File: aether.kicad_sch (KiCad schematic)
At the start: 41 parts, among them J2 USB_C_Receptacle_USB2.0, Q1 NPN, Q2 NPN, Q3 NPN, Q4 NPN, Q5 NPN, SW1 SW_SPDT, SW3 SW_Push, U13 STM32F405RGTx, U4 USBLC6-2SC6, Y1 25MHz

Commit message: updated footprint library
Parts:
- C24, C25, C26, C27, C28, C35, C42: footprint Capacitor_SMD:C_0201_0603Metric -> Capacitor_SMD:C_0402_1005Metric
- C36, C41: footprint (none) -> Capacitor_SMD:C_0402_1005Metric
- R10, R9: footprint Resistor_SMD:R_0201_0603Metric -> Resistor_SMD:R_0402_1005Metric
- R33, R35, R37, R39, R41, R42, R43, R44, R52: footprint (none) -> Resistor_SMD:R_0402_1005Metric
- RN1: footprint (none) -> 742C083274JP:RESCAV80P320X160X70-8N
- RN2: footprint (none) -> YC164-JR-0747KL:RESCAXE80P320X160X70-8N
- RN4: footprint (none) -> YC164-JR-0710KL:RESCAXE80P320X160X70-8N
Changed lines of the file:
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@@
       (effects (font (size 1.27 1.27)))
     )
-    (property "Footprint" "" (at 243.84 104.775 90)
+    (property "Footprint" "YC164-JR-0710KL:RESCAXE80P320X160X70-8N" (at 243.84 104.775 90)
       (effects (font (size 1.27 1.27)) hide)
     )
@@
       (effects (font (size 1.27 1.27)) (justify left))
     )
-    (property "Footprint" "Capacitor_SMD:C_0201_0603Metric" (at 51.7652 186.69 0)
+    (property "Footprint" "Capacitor_SMD:C_0402_1005Metric" (at 51.7652 186.69 0)
       (effects (font (size 1.27 1.27)) hide)
     )
@@
       (effects (font (size 1.27 1.27)))
     )
-    (property "Footprint" "" (at 145.7452 110.49 0)
+    (property "Footprint" "Capacitor_SMD:C_0402_1005Metric" (at 145.7452 110.49 0)
       (effects (font (size 1.27 1.27)) hide)
     )
@@
       (effects (font (size 1.27 1.27)) (justify left))
     )
-    (property "Footprint" "" (at 143.002 97.79 90)
+    (property "Footprint" "Resistor_SMD:R_0402_1005Metric" (at 143.002 97.79 90)
       (effects (font (size 1.27 1.27)) hide)
     )
@@
       (effects (font (size 1.27 1.27)) (justify left))
     )
-    (property "Footprint" "Capacitor_SMD:C_0201_0603Metric" (at 105.1052 186.69 0)
+    (property "Footprint" "Capacitor_SMD:C_0402_1005Metric" (at 105.1052 186.69 0)
       (effects (font (size 1.27 1.27)) hide)
     )
@@
       (effects (font (size 1.27 1.27)))
     )
-    (property "Footprint" "" (at 243.84 125.222 90)
+    (property "Footprint" "Resistor_SMD:R_0402_1005Metric" (at 243.84 125.222 90)
       (effects (font (size 1.27 1.27)) hide)
     )
@@
       (effects (font (size 1.27 1.27)) (justify left))
     )
-    (property "Footprint" "Capacitor_SMD:C_0201_0603Metric" (at 202.8952 144.78 0)
+    (property "Footprint" "Capacitor_SMD:C_0402_1005Metric" (at 202.8952 144.78 0)
       (effects (font (size 1.27 1.27)) hide)
     )
@@
       (effects (font (size 1.27 1.27)) (justify left))
     )
-    (property "Footprint" "" (at 252.095 45.72 90)
+    (property "Footprint" "YC164-JR-0747KL:RESCAXE80P320X160X70-8N" (at 252.095 45.72 90)
       (effects (font (size 1.27 1.27)) hide)
     )
@@
       (effects (font (size 1.27 1.27)))
     )
-    (property "Footprint" "" (at 243.84 141.732 90)
+    (property "Footprint" "Resistor_SMD:R_0402_1005Metric" (at 243.84 141.732 90)
       (effects (font (size 1.27 1.27)) hide)
     )
@@
       (effects (font (size 1.27 1.27)))
     )
-    (property "Footprint" "Resistor_SMD:R_0201_0603Metric" (at 204.47 42.418 90)
+    (property "Footprint" "Resistor_SMD:R_0402_1005Metric" (at 204.47 42.418 90)
       (effects (font (size 1.27 1.27)) hide)
     )
@@
       (effects (font (size 1.27 1.27)) (justify left))
     )
-    (property "Footprint" "Capacitor_SMD:C_0201_0603Metric" (at 148.2852 185.42 0)
+    (property "Footprint" "Capacitor_SMD:C_0402_1005Metric" (at 148.2852 185.42 0)
       (effects (font (size 1.27 1.27)) hide)
     )
@@
       (effects (font (size 1.27 1.27)))
     )
-    (property "Footprint" "" (at 243.84 97.282 90)
+    (property "Footprint" "Resistor_SMD:R_0402_1005Metric" (at 243.84 97.282 90)
       (effects (font (size 1.27 1.27)) hide)
     )
@@
       (effects (font (size 1.27 1.27)))
     )
-    (property "Footprint" "" (at 255.27 42.545 90)
+    (property "Footprint" "742C083274JP:RESCAV80P320X160X70-8N" (at 255.27 42.545 90)
       (effects (font (size 1.27 1.27)) hide)
     )
@@
       (effects (font (size 1.27 1.27)))
     )
-    (property "Footprint" "" (at 193.04 94.488 90)
+    (property "Footprint" "Resistor_SMD:R_0402_1005Metric" (at 193.04 94.488 90)
       (effects (font (size 1.27 1.27)) hide)
     )
@@
       (effects (font (size 1.27 1.27)) (justify left))
     )
-    (property "Footprint" "Capacitor_SMD:C_0201_0603Metric" (at 69.5452 186.69 0)
+    (property "Footprint" "Capacitor_SMD:C_0402_1005Metric" (at 69.5452 186.69 0)
       (effects (font (size 1.27 1.27)) hide)
     )
@@
       (effects (font (size 1.27 1.27)) (justify right))
     )
-    (property "Footprint" "" (at 189.738 97.79 90)
+    (property "Footprint" "Resistor_SMD:R_0402_1005Metric" (at 189.738 97.79 90)
       (effects (font (size 1.27 1.27)) hide)
     )
@@
       (effects (font (size 1.27 1.27)))
     )
-    (property "Footprint" "" (at 243.84 80.772 90)
+    (property "Footprint" "Resistor_SMD:R_0402_1005Metric" (at 243.84 80.772 90)
       (effects (font (size 1.27 1.27)) hide)
     )
@@
       (effects (font (size 1.27 1.27)) (justify left))
     )
-    (property "Footprint" "Capacitor_SMD:C_0201_0603Metric" (at 33.9852 186.69 0)
+    (property "Footprint" "Capacitor_SMD:C_0402_1005Metric" (at 33.9852 186.69 0)
       (effects (font (size 1.27 1.27)) hide)
     )
@@
       (effects (font (size 1.27 1.27)))
     )
-    (property "Footprint" "" (at 126.0348 102.87 0)
+    (property "Footprint" "Capacitor_SMD:C_0402_1005Metric" (at 126.0348 102.87 0)
       (effects (font (size 1.27 1.27)) hide)
     )
@@
       (effects (font (size 1.27 1.27)))
     )
-    (property "Footprint" "Resistor_SMD:R_0201_0603Metric" (at 204.47 36.322 90)
+    (property "Footprint" "Resistor_SMD:R_0402_1005Metric" (at 204.47 36.322 90)
       (effects (font (size 1.27 1.27)) hide)
     )
@@
       (effects (font (size 1.27 1.27)))
     )
-    (property "Footprint" "" (at 38.1 121.158 90)
+    (property "Footprint" "Resistor_SMD:R_0402_1005Metric" (at 38.1 121.158 90)
       (effects (font (size 1.27 1.27)) hide)
     )
@@
       (effects (font (size 1.27 1.27)))
     )
-    (property "Footprint" "" (at 121.92 139.192 90)
+    (property "Footprint" "Resistor_SMD:R_0402_1005Metric" (at 121.92 139.192 90)
       (effects (font (size 1.27 1.27)) hide)
     )
@@
       (effects (font (size 1.27 1.27)) (justify left))
     )
-    (property "Footprint" "Capacitor_SMD:C_0201_0603Metric" (at 87.3252 186.69 0)
-      (effects (font (size 1.27 1.27)) hide)
-    )
+    (property "Footprint" "Capacitor_SMD:C_0402_1005Metric" (at 87.3252 186.69 0)
+      (effects (font (size 1.27 1.27)) hide)
+    )

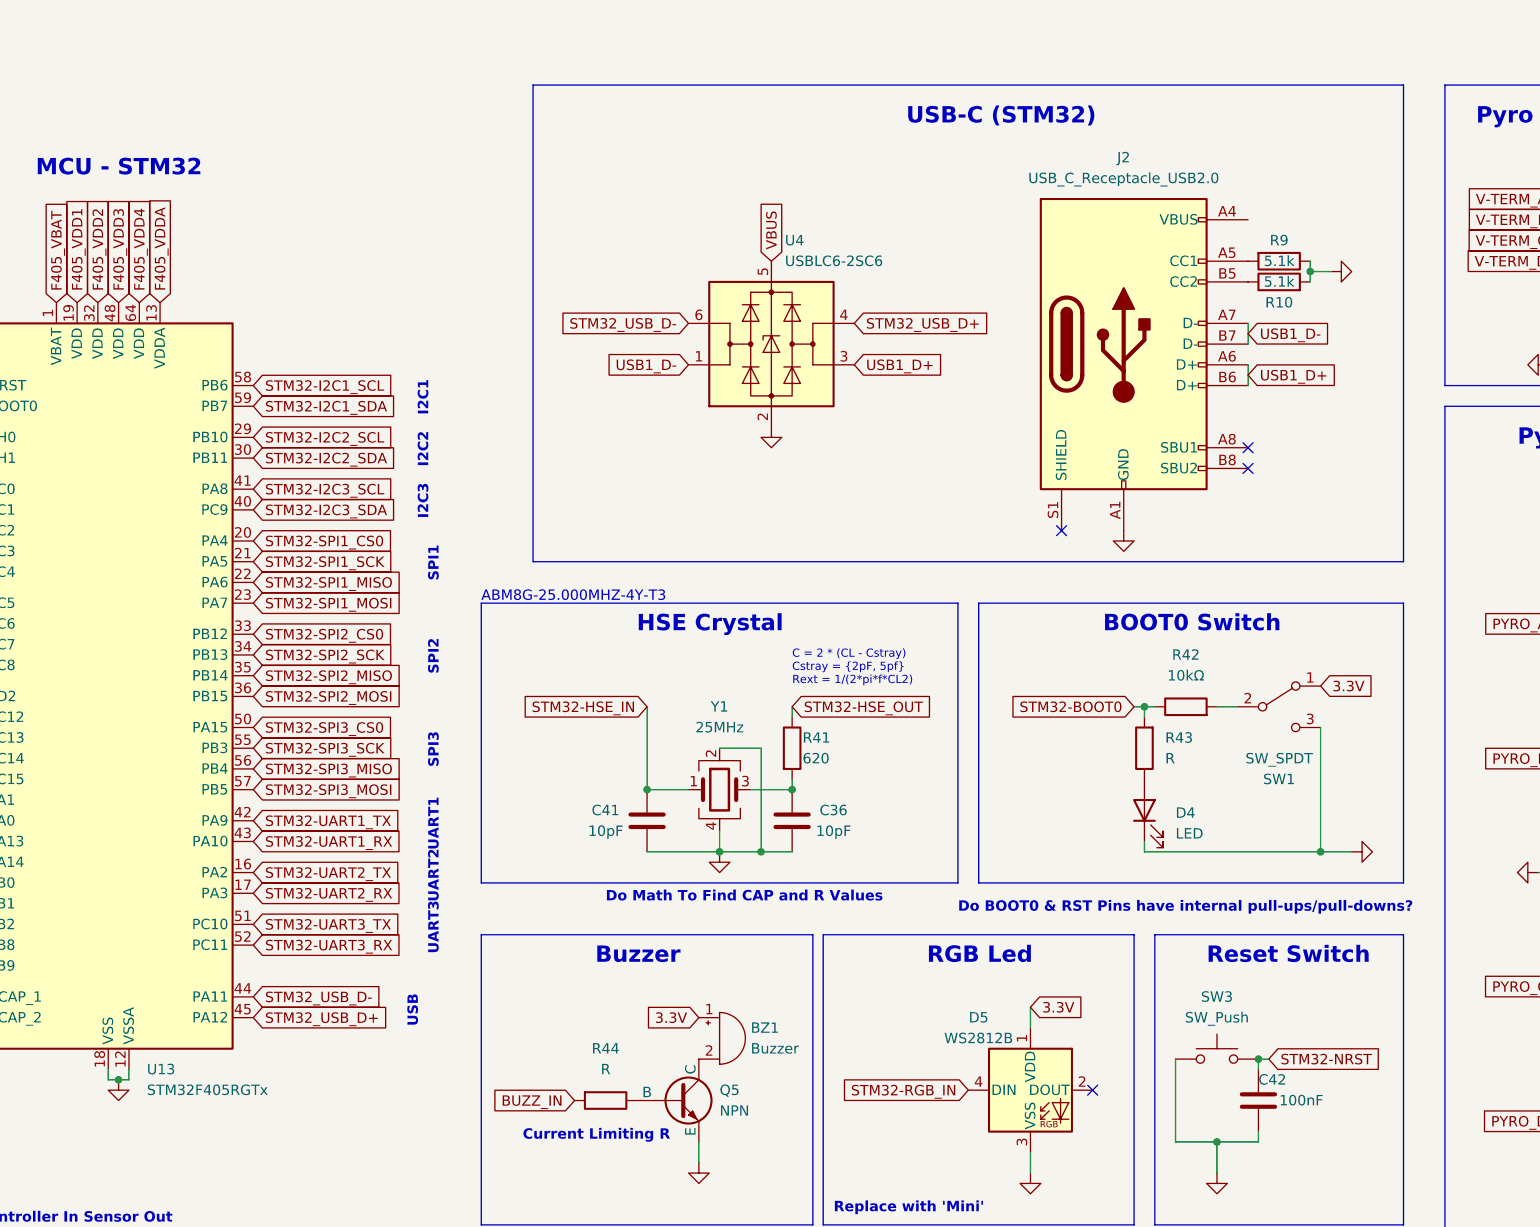
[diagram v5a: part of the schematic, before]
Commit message: Updated symbol footprints
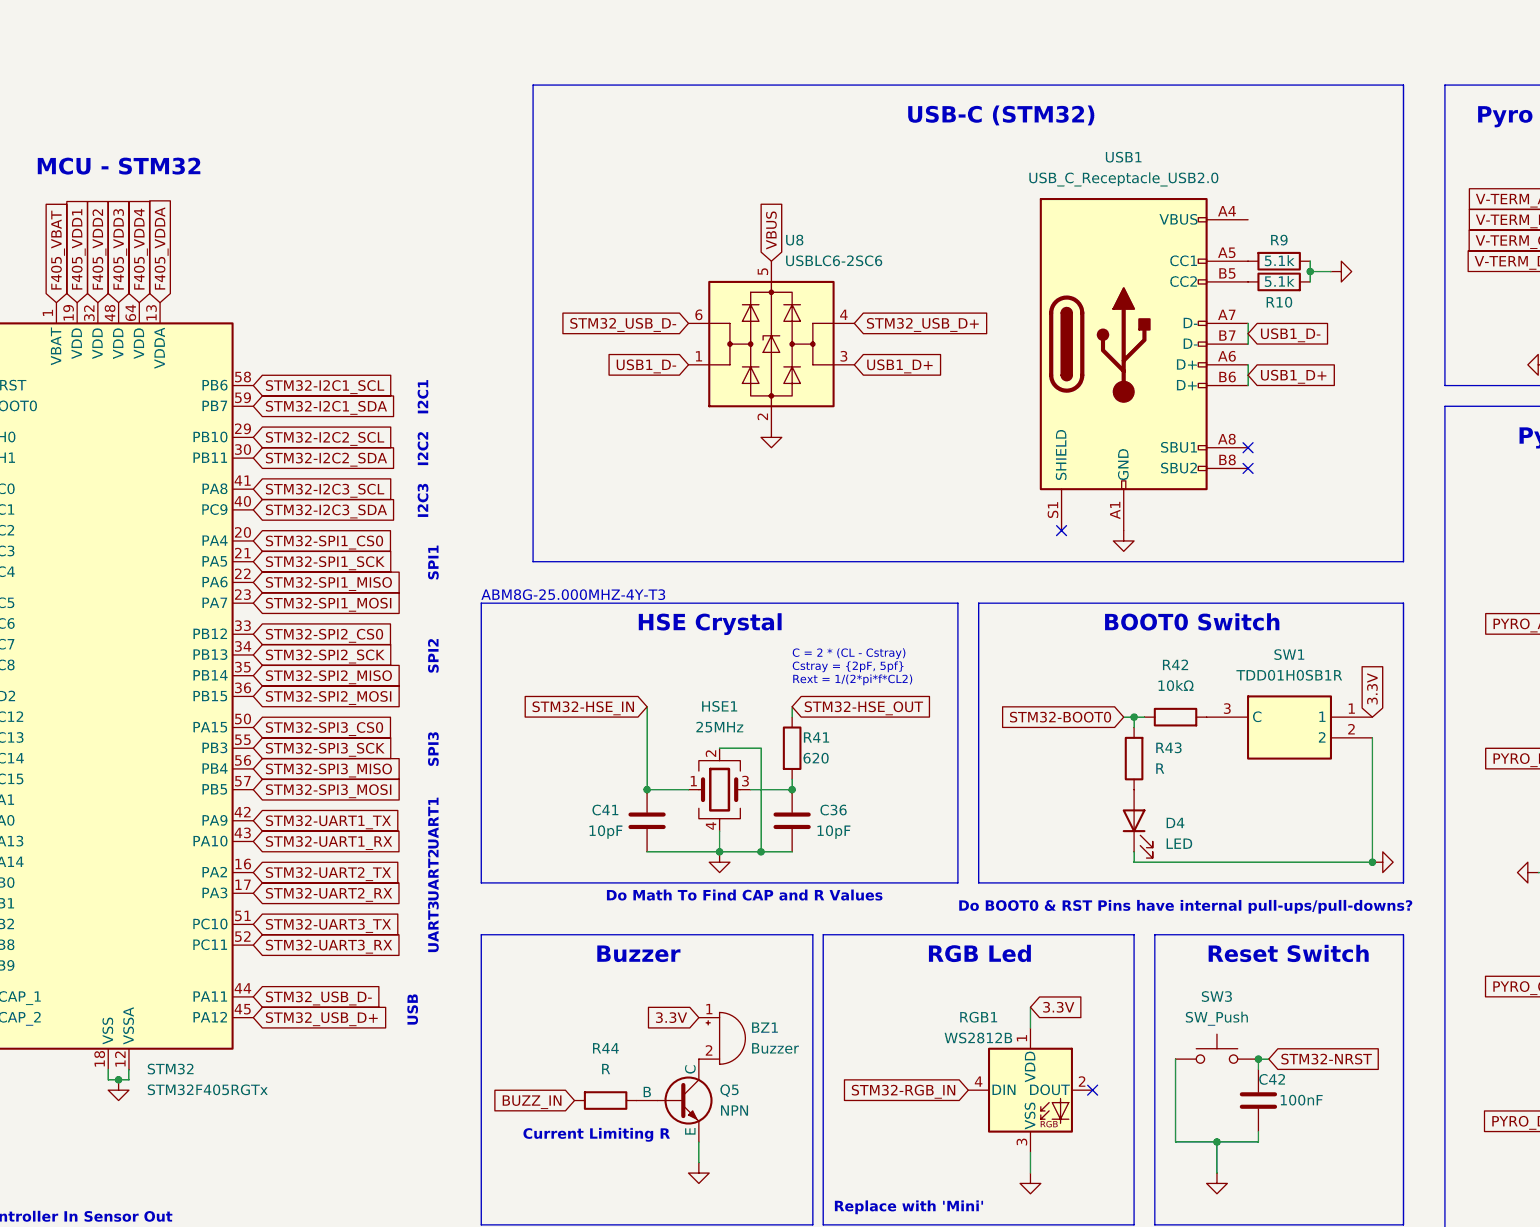
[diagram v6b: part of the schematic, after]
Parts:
- removed SW1: SW_SPDT, symbol Switch:SW_SPDT
- added SW1: TDD01H0SB1R, TDD01H0SB1R:SOT175P420X230-3N, symbol TDD01H0SB1R:TDD01H0SB1R
- C34, C37, C38: footprint Capacitor_SMD:C_0201_0603Metric -> Capacitor_SMD:C_0603_1608Metric
- D4: footprint (none) -> LED_SMD:LED_0603_1608Metric
- FB1: footprint (none) -> Inductor_SMD:L_0402_1005Metric
- HSE1: renamed from Y1; footprint (none) -> Crystal:Crystal_SMD_Abracon_ABM8G-4Pin_3.2x2.5mm
- R10, R33, R35, R37, R39, R41, R42, R43, R44, R52, R9: footprint Resistor_SMD:R_0402_1005Metric -> Resistor_SMD:R_0603_1608Metric
- USB1: renamed from J2; footprint (none) -> Connector_USB:USB_C_Receptacle_GCT_USB4105-xx-A_16P_TopMnt_Horizontal
- renumbered D5 to RGB1, U13 to STM32, U4 to U8
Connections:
- net 3.3V: now also SW1.1
- net GND: now also SW1.2
- net at R42.2: now also SW1.3 (C)
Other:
- moved on the sheet: D4, R42, R43

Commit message: updated schematic
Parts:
- removed Q1, Q2, Q3, Q4: NPN, symbol Simulation_SPICE:NPN
- removed SW3: SW_Push, symbol Switch:SW_Push
- added Q2, Q3, Q4, Q5: CSD17575Q3, CSD17575Q3:TRANS_CSD17308Q3, symbol CSD17575Q3:CSD17575Q3
- added SW?: PTS526_SM08_SMTR2_LFS, PTS526_SM08_SMTR2_LFS:SW_PTS526_SM08_SMTR2_LFS, symbol PTS526_SM08_SMTR2_LFS:PTS526_SM08_SMTR2_LFS
- BZ1: footprint (none) -> CSS-0575A-SMT:CUI_CSS-0575A-SMT
- Q1: renamed from Q5; footprint (none) -> Package_TO_SOT_SMD:SOT-23
- R2: renamed from R44; value R -> 1k
- renumbered C37 to C1, C36 to C10, C35 to C11, C42 to C12, C24 to C2, C38 to C3, C25 to C4, C26 to C5, C27 to C6, C28 to C7, C41 to C8, C34 to C9, D4 to D1, R52 to R1, R37 to R10, R39 to R11, R41 to R3, R43 to R4, R42 to R5, R9 to R6, R10 to R7, R33 to R8, R35 to R9, RN4 to RN1, RN1 to RN3, STM32 to STM1, U8 to U1
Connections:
- net GND: now also Q2.1 (S), Q2.2 (S), Q2.3 (S), Q3.1 (S), Q3.2 (S), Q3.3 (S), Q4.1 (S), Q4.2 (S), Q4.3 (S), Q5.1 (S), Q5.2 (S), Q5.3 (S), SW?.1, SW?.2
- net PYRO-TERM_A: now also Q2.5 (D), Q2.6 (D), Q2.7 (D), Q2.8 (D), Q2.9 (D)
- net PYRO-TERM_B: now also Q3.5 (D), Q3.6 (D), Q3.7 (D), Q3.8 (D), Q3.9 (D)
- net PYRO-TERM_C: now also Q4.5 (D), Q4.6 (D), Q4.7 (D), Q4.8 (D), Q4.9 (D)
- net PYRO-TERM_D: now also Q5.5 (D), Q5.6 (D), Q5.7 (D), Q5.8 (D), Q5.9 (D)
- net STM32-NRST: now also SW?.3, SW?.4
- net at R11.1, RN1.1 (R1.1): now also Q5.4 (G)
- net at R10.1, RN1.2 (R2.1): now also Q4.4 (G)
- net at R9.1, RN1.3 (R3.1): now also Q3.4 (G)
- net at R8.1, RN1.4 (R4.1): now also Q2.4 (G)

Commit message: updated pcb
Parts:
- removed BZ1: Buzzer, CSS-0575A-SMT:CUI_CSS-0575A-SMT, symbol Device:Buzzer
- added BZ1: CSS-0575A-SMT, CSS-0575A-SMT:CUI_CSS-0575A-SMT, symbol CSS-0575A-SMT:CSS-0575A-SMT
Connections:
- net 3.3V: now also BZ1.1
- net at Q1.1 (C): now also BZ1.2
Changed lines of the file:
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@@
+    (stroke (width 0) (type default))
+  )
+  (wire (pts (xy 135.89 125.73) (xy 133.35 125.73))
     (stroke (width 0) (type default))
   )
@@
   )
   (wire (pts (xy 245.11 50.8) (xy 247.65 50.8))
+    (stroke (width 0) (type default))
+  )
+  (wire (pts (xy 135.89 135.89) (xy 133.35 135.89))
     (stroke (width 0) (type default))
   )
@@
     )
   )
-  (global_label "3.3V" (shape input) (at 133.35 130.81 180) (fields_autoplaced)
-    (effects (font (size 1.27 1.27)) (justify right))
-    (property "Intersheetrefs" "${INTERSHEET_REFS}" (at 126.2524 130.81 0)
+  (global_label "3.3V" (shape input) (at 133.35 125.73 180) (fields_autoplaced)
+    (effects (font (size 1.27 1.27)) (justify right))
+    (property "Intersheetrefs" "${INTERSHEET_REFS}" (at 126.2524 125.73 0)
       (effects (font (size 1.27 1.27)) (justify right) hide)
     )
@@
     )
   )
-  (symbol (lib_id "Device:Buzzer") (at 135.89 133.35 0) (unit 1)
-    (in_bom yes) (on_board yes) (dnp no)
-    (property "Reference" "BZ1" (at 139.7 132.08 0)
-      (effects (font (size 1.27 1.27)) (justify left))
-    )
-    (property "Value" "Buzzer" (at 139.7 134.62 0)
-      (effects (font (size 1.27 1.27)) (justify left))
-    )
-    (property "Footprint" "CSS-0575A-SMT:CUI_CSS-0575A-SMT" (at 135.255 130.81 90)
-      (effects (font (size 1.27 1.27)) hide)
-    )
-    (property "Datasheet" "~" (at 135.255 130.81 90)
-      (effects (font (size 1.27 1.27)) hide)
-    )
-    (pin "1")
+  (symbol (lib_id "CSS-0575A-SMT:CSS-0575A-SMT") (at 135.89 130.81 0) (unit 1)
+    (in_bom yes) (on_board yes) (dnp no) (fields_autoplaced)
+    (property "Reference" "BZ1" (at 139.7 130.7399 0)
+      (effects (font (size 1.27 1.27)) (justify left))
+    )
+    (property "Value" "CSS-0575A-SMT" (at 139.7 132.0099 0)
+      (effects (font (size 1.27 1.27)) (justify left) hide)
+    )
+    (property "Footprint" "CSS-0575A-SMT:CUI_CSS-0575A-SMT" (at 135.89 130.81 0)
+      (effects (font (size 1.27 1.27)) (justify bottom) hide)
+    )
+    (property "Datasheet" "" (at 135.89 130.81 0)
+      (effects (font (size 1.27 1.27)) hide)
+    )
+    (property "MF" "CUI Devices" (at 135.89 130.81 0)
+      (effects (font (size 1.27 1.27)) (justify bottom) hide)
+    )
+    (property "DESCRIPTION" "5 mm, 3 V, 75 dB, Surface Mount _SMT_, Magnetic Audio Transducer Buzzer" (at 135.89 130.81 0)
+      (effects (font (size 1.27 1.27)) (justify bottom) hide)
+    )
+    (property "PACKAGE" "None" (at 135.89 130.81 0)
+      (effects (font (size 1.27 1.27)) (justify bottom) hide)
+    )
+    (property "PRICE" "None" (at 135.89 130.81 0)
+      (effects (font (size 1.27 1.27)) (justify bottom) hide)
+    )
+    (property "Package" "CUI Devices" (at 135.89 130.81 0)
+      (effects (font (size 1.27 1.27)) (justify bottom) hide)
+    )
+    (property "Check_prices" "https://www.snapeda.com/parts/CSS-0575A-SMT-TR/CUI+Devices/view-part/?ref=eda" (at 135.89 130.81 0)
+      (effects (font (size 1.27 1.27)) (justify bottom) hide)
+    )
+    (property "Price" "None" (at 135.89 130.81 0)
+      (effects (font (size 1.27 1.27)) (justify bottom) hide)
+    )
+    (property "SnapEDA_Link" "https://www.snapeda.com/parts/CSS-0575A-SMT-TR/CUI+Devices/view-part/?ref=snap" (at 135.89 130.81 0)
+      (effects (font (size 1.27 1.27)) (justify bottom) hide)
+    )
+    (property "MP" "CSS-0575A-SMT-TR" (at 135.89 130.81 0)
+      (effects (font (size 1.27 1.27)) (justify bottom) hide)
+    )
+    (property "Purchase-URL" "https://www.snapeda.com/api/url_track_click_mouser/?unipart_id=5633932&manufacturer=CUI Devices&part_name=CSS-0575A-SMT-TR&search_term=buzzer 3v" (at 135.89 130.81 0)
+      (effects (font (size 1.27 1.27)) (justify bottom) hide)
+    )
+    (property "Availability" "In Stock" (at 135.89 130.81 0)
+      (effects (font (size 1.27 1.27)) (justify bottom) hide)
+    )
+    (property "CUI_purchase_URL" "https://www.cuidevices.com/product/audio/buzzers/audio-transducers/css-0575a-smt-tr?utm_source=snapeda.com&utm_medium=referral&utm_campaign=snapedaBOM" (at 135.89 130.81 0)
+      (effects (font (size 1.27 1.27)) (justify bottom) hide)
+    )
+    (property "AVAILABILITY" "Unavailable" (at 135.89 130.81 0)
+      (effects (font (size 1.27 1.27)) (justify bottom) hide)
+    )
+    (property "Description" "5 mm, 3 V, 76 dB, Surface Mount (SMT), Magnetic Audio Transducer Buzzer" (at 135.89 130.81 0)
+      (effects (font (size 1.27 1.27)) (justify bottom) hide)
+    )
+    (pin "1")
